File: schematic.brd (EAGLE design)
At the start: 100 x 80 mm, 40 parts, among them IC1 PIC16F877P, T1 2N2222, T2 2N2222

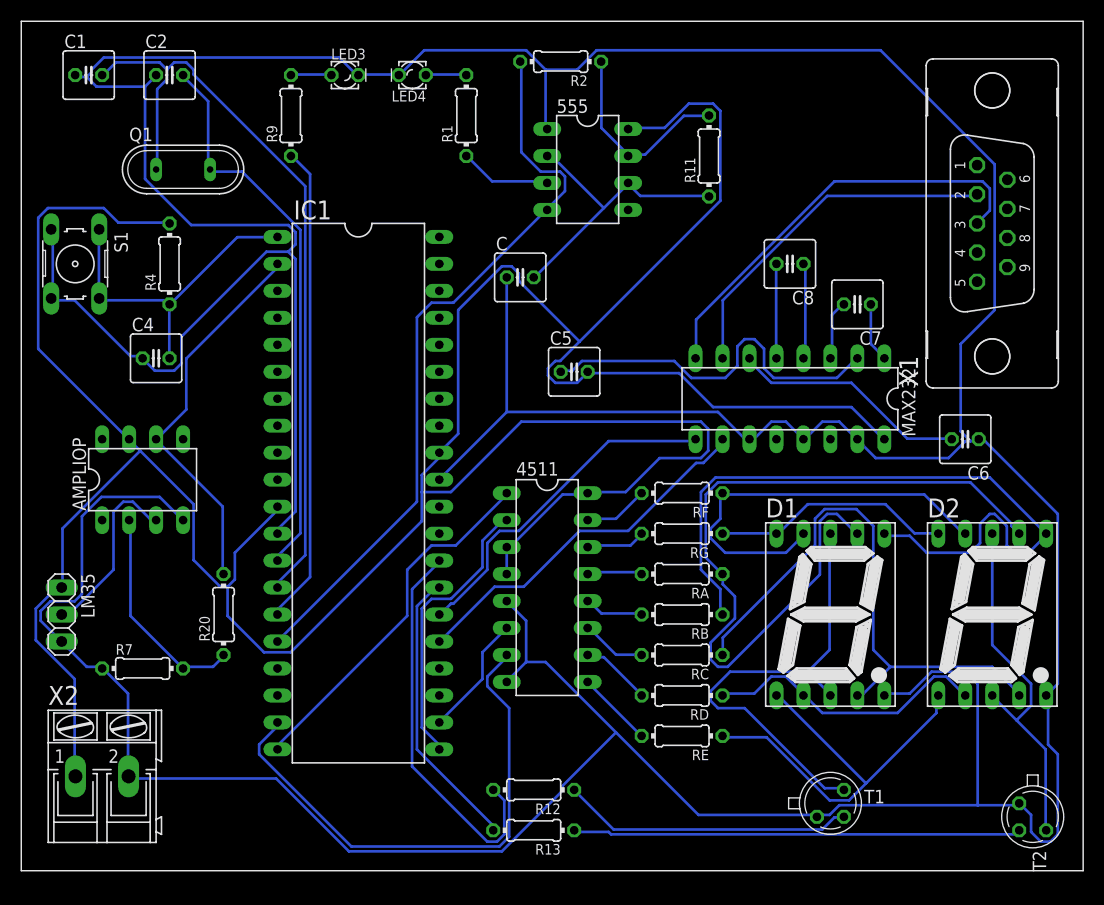
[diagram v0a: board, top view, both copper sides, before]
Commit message: correction to board + plan de masse
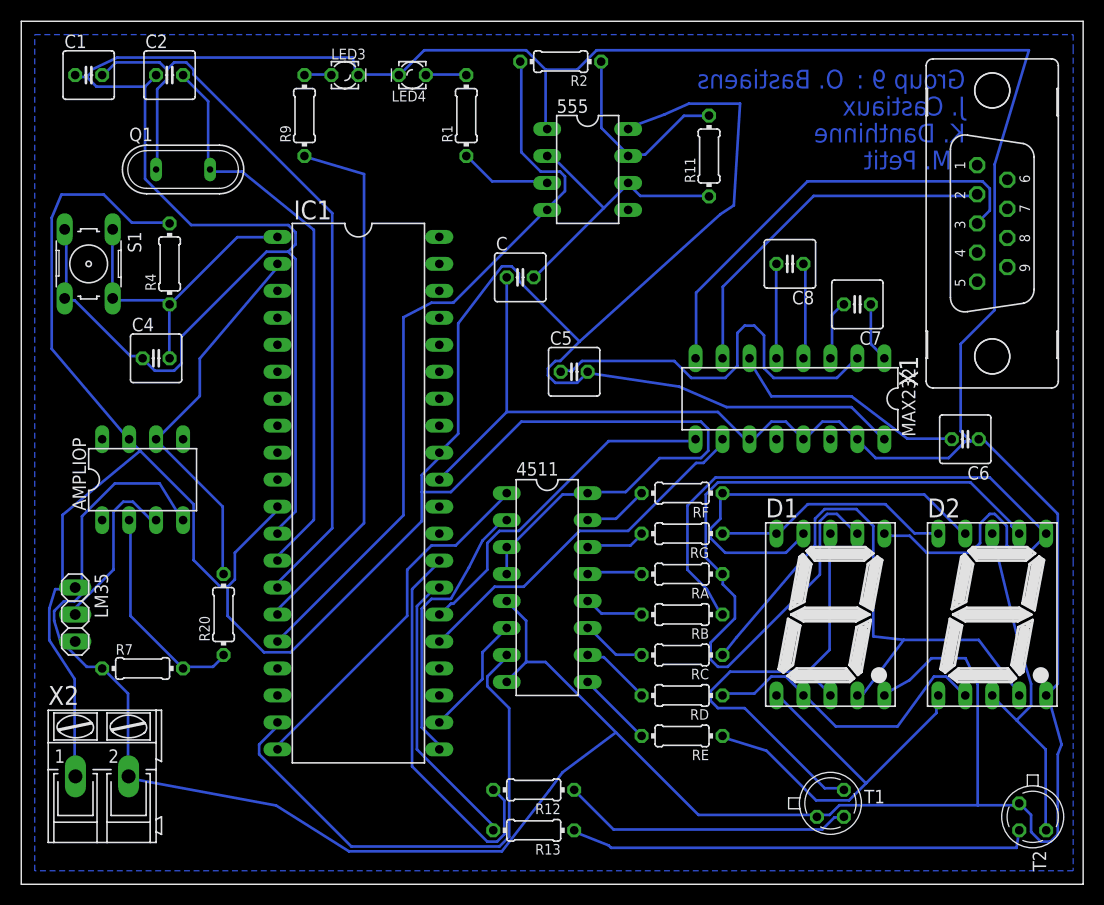
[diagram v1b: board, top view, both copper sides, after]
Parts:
- moved R9 1.27 mm to (26.7, 71.1)
- moved LM35 1.27 mm to (5.08, 24.1)
- moved S1 1.27 mm to (6.35, 57.1)
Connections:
- net N$40 renamed GND
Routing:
- net GND: track 528.6 -> 539.5 mm
- net N$13: track 45.2 -> 50.7 mm
- net N$17: track 34.9 -> 37.5 mm
- net N$46: track 301.9 -> 304.3 mm
- net N$2: track 74.0 -> 76.1 mm
- net N$38: track 54.5 -> 56.4 mm
- net N$37: track 27.3 -> 28.8 mm
- net N$16: track 40.7 -> 42.2 mm
- net N$8: track 53.0 -> 54.5 mm
- net N$48: track 42.3 -> 43.8 mm
- net N$7: track 31.3 -> 30.0 mm
- net N$10: track 3.82 -> 2.55 mm
- net N$47: track 34.5 -> 33.4 mm
- net N$51: track 69.7 -> 70.6 mm
- net N$15: track 33.5 -> 34.3 mm
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- added copper zone on layer 16, net GND
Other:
- board size 100 x 80 mm -> 100 x 81.3 mm
- board text added: "Group 9 :"
- board text added: "J. Castiaux"
- board text added: "K. Danthinne"
- board text added: "M. Petit"
- board text added: "O. Bastiaens"
